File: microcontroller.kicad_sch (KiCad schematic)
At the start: 20 parts, among them SW1 A6S-2104-H, U6 STM32H725RGV6, Y1 ECS-2520MV-240-BN

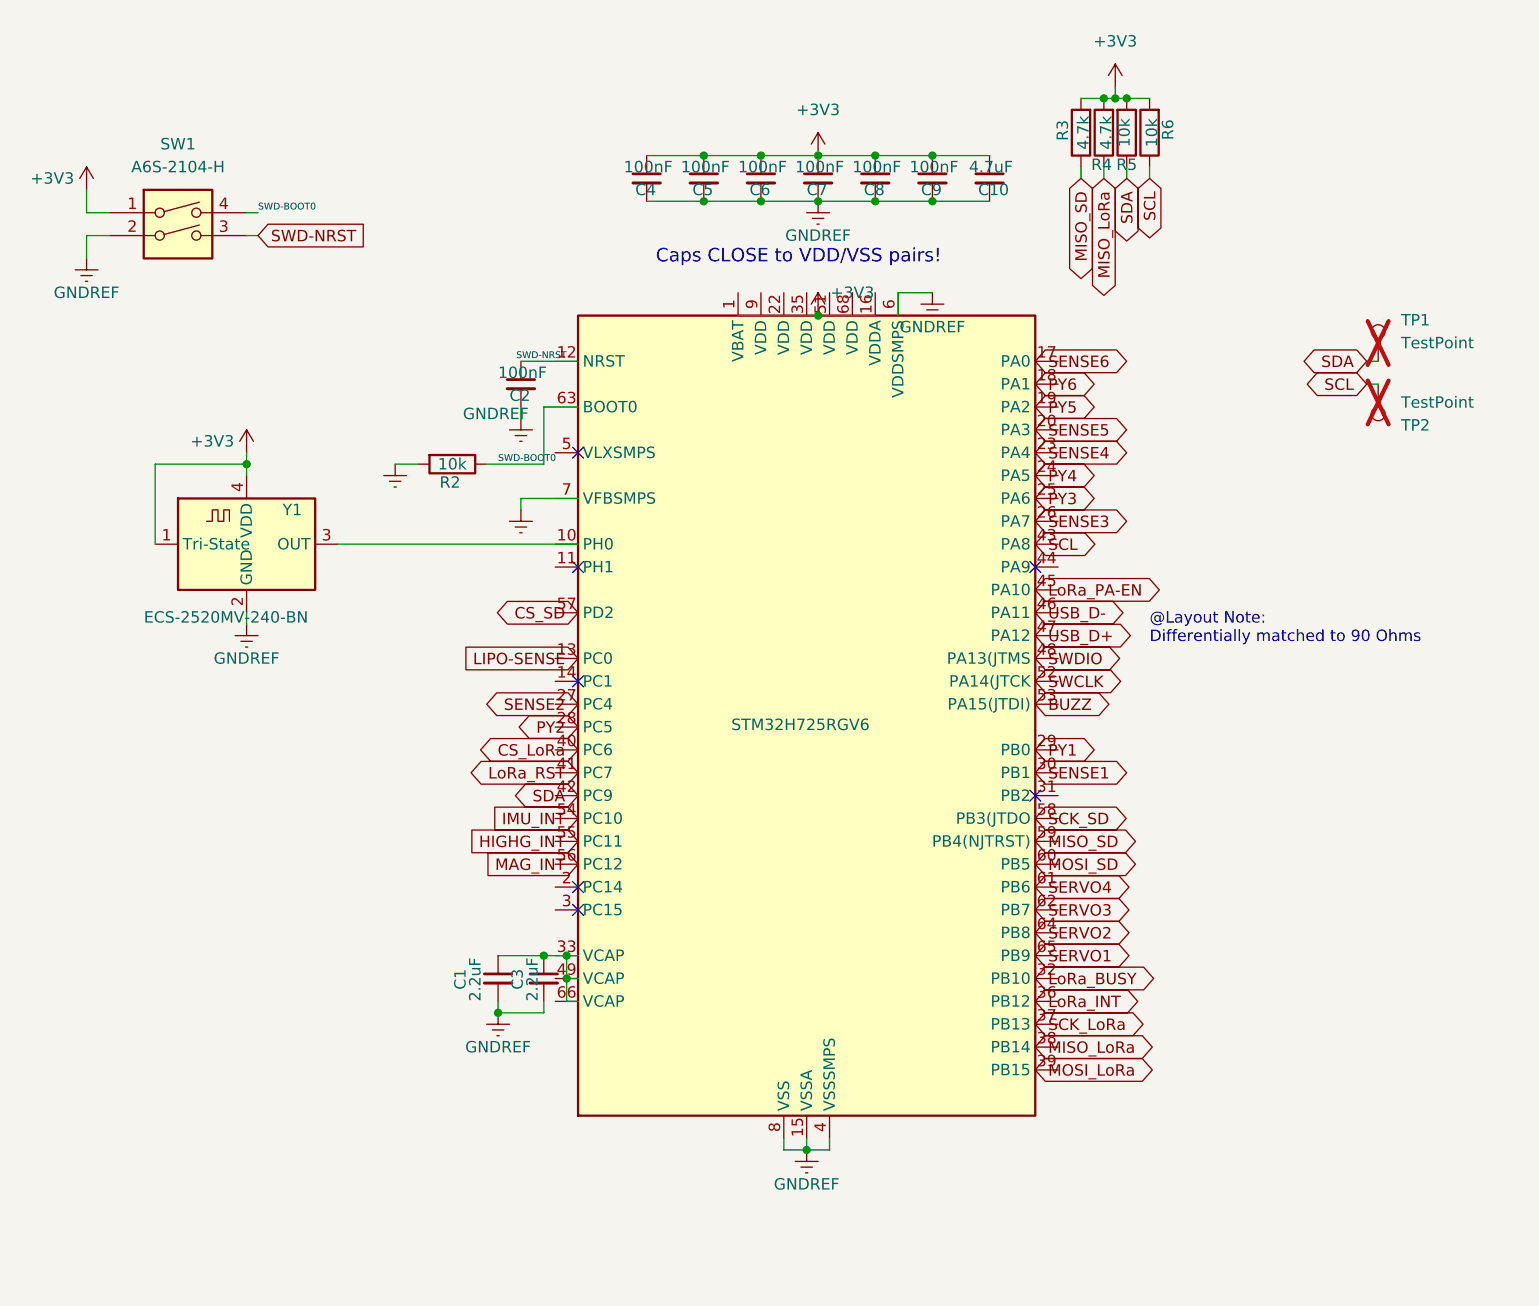
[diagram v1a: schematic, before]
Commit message: Added previously missing V_CORE 1.35V regulator
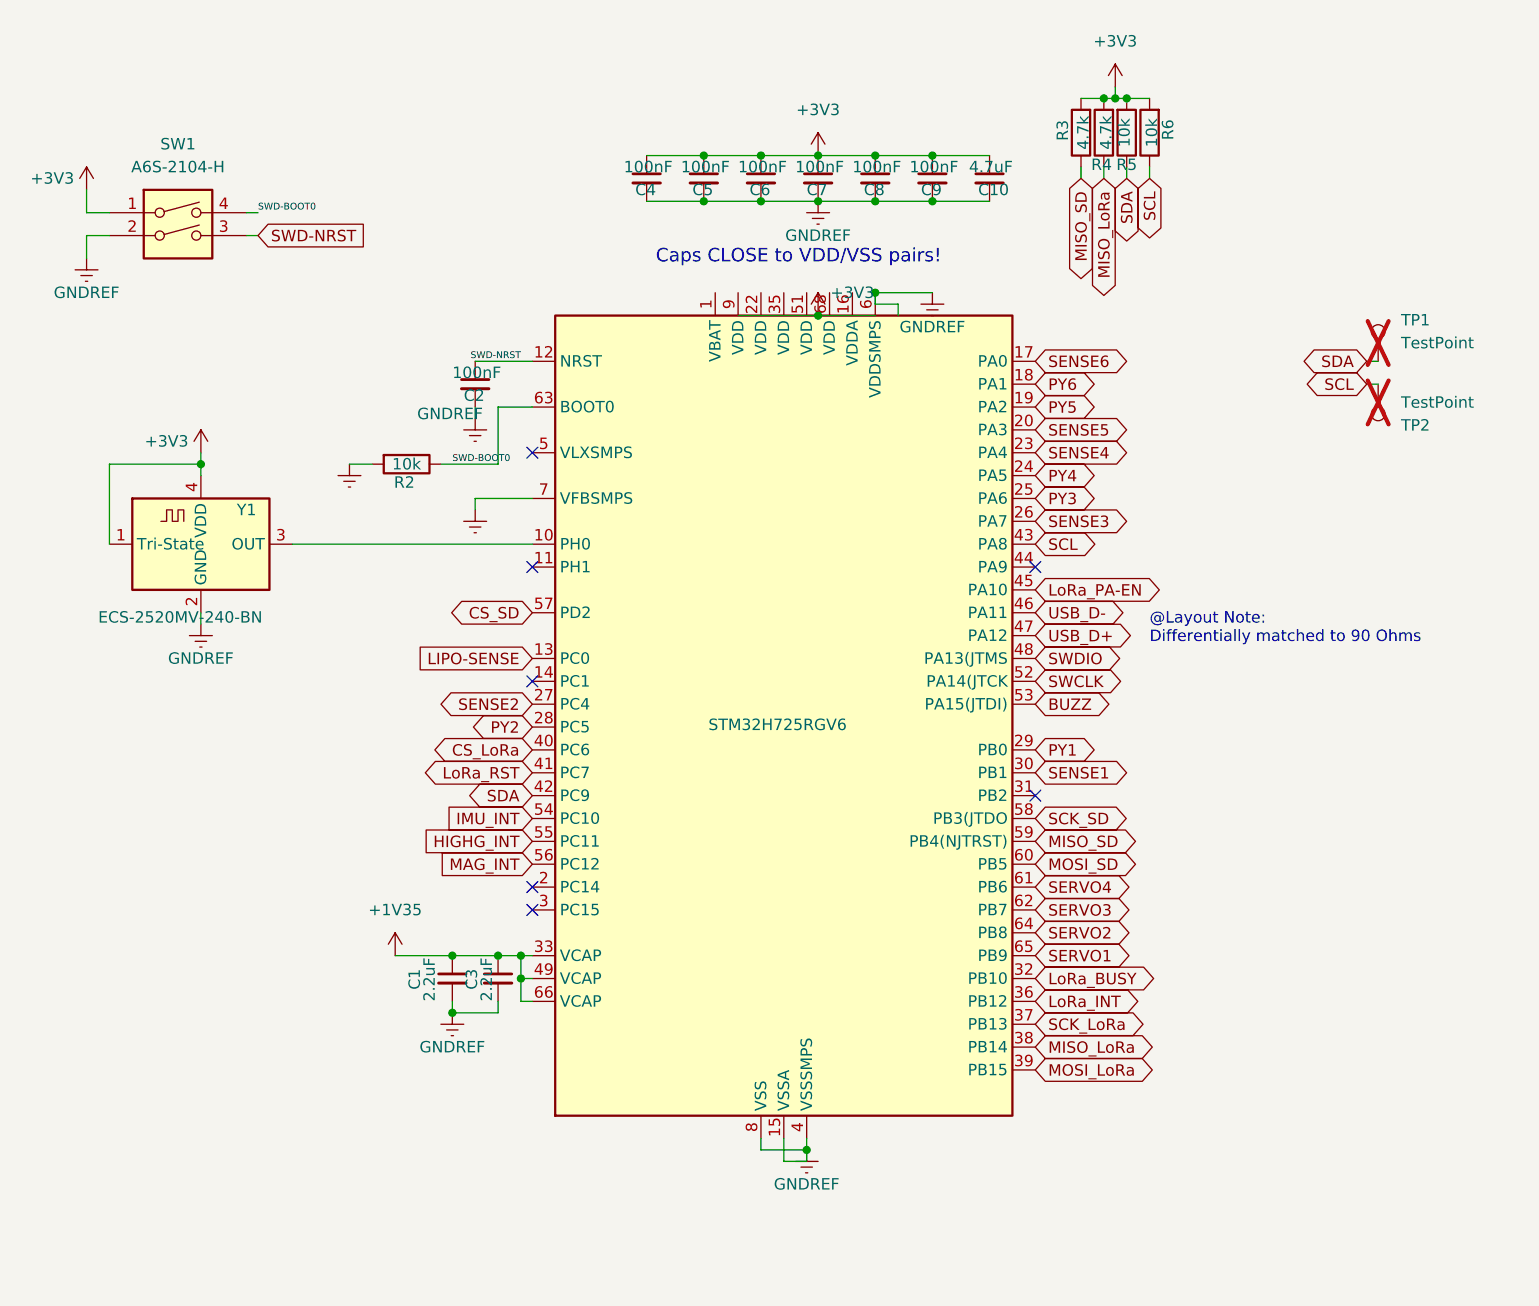
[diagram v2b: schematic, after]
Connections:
- net BUZZ: now also U6.53 (PA15(JTDI))
- net CS_LoRa: now also U6.40 (PC6)
- net CS_SD: now also U6.57 (PD2)
- net GNDREF: now also U6.7 (VFBSMPS)
- net HIGHG_INT: now also U6.55 (PC11)
- net IMU_INT: now also U6.54 (PC10)
- net LIPO-SENSE: now also U6.13 (PC0)
- net LoRa_BUSY: now also U6.32 (PB10)
- net LoRa_INT: now also U6.36 (PB12)
- net LoRa_PA-EN: now also U6.45 (PA10)
- net LoRa_RST: now also U6.41 (PC7)
- net MAG_INT: now also U6.56 (PC12)
- net MISO_LoRa: now also U6.38 (PB14)
- net MISO_SD: now also U6.59 (PB4(NJTRST))
- net MOSI_LoRa: now also U6.39 (PB15)
- net MOSI_SD: now also U6.60 (PB5)
- net PY1: now also U6.29 (PB0)
- net PY2: now also U6.28 (PC5)
- net PY3: now also U6.25 (PA6)
- net PY4: now also U6.24 (PA5)
- net PY5: now also U6.19 (PA2)
- net PY6: now also U6.18 (PA1)
- net SCK_LoRa: now also U6.37 (PB13)
- net SCK_SD: now also U6.58 (PB3(JTDO)
- net SCL: now also U6.43 (PA8)
- net SDA: now also U6.42 (PC9)
- net SENSE1: now also U6.30 (PB1)
- net SENSE2: now also U6.27 (PC4)
- net SENSE3: now also U6.26 (PA7)
- net SENSE4: now also U6.23 (PA4)
- net SENSE5: now also U6.20 (PA3)
- net SENSE6: now also U6.17 (PA0)
- net SERVO1: now also U6.65 (PB9)
- net SERVO2: now also U6.64 (PB8)
- net SERVO3: now also U6.62 (PB7)
- net SERVO4: now also U6.61 (PB6)
- net SWCLK: now also U6.52 (PA14(JTCK)
- net SWD-BOOT0: now also U6.63 (BOOT0)
- net SWD-NRST: now also U6.12 (NRST)
- net SWDIO: now also U6.48 (PA13(JTMS)
- net USB_D+: now also U6.47 (PA12)
- net USB_D-: now also U6.46 (PA11)
- net +1V35: now reaches C1.1, C3.1
- net +1V35: now also U6.33 (VCAP), U6.49 (VCAP), U6.66 (VCAP)
- net at U6.10 (PH0): now also Y1.3 (OUT)
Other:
- moved on the sheet: C1, C2, C3, R2, Y1

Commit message: Some layout tweaks
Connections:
- net +3V3: now also U6.1 (VBAT), U6.16 (VDDA), U6.22 (VDD), U6.35 (VDD), U6.51 (VDD), U6.68 (VDD), U6.9 (VDD)

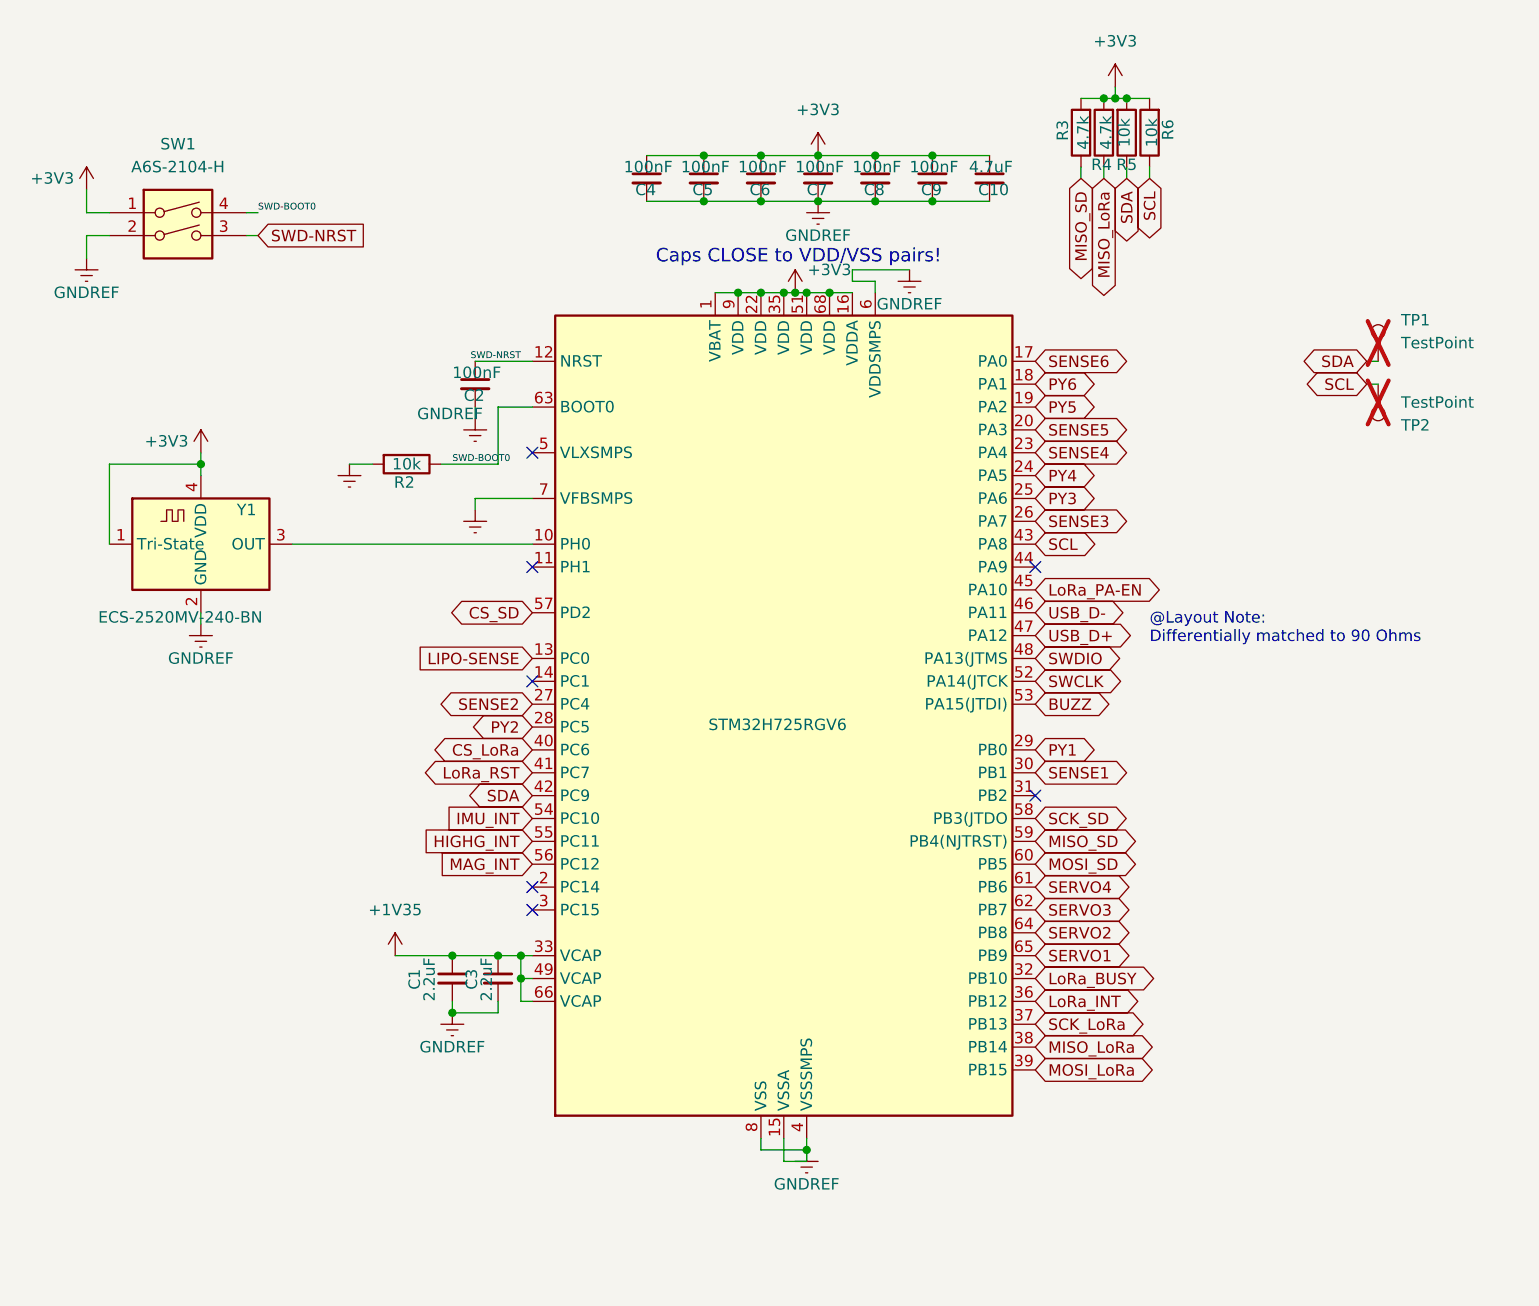
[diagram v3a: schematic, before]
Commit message: updated power delivery and component choices. v4 now ready
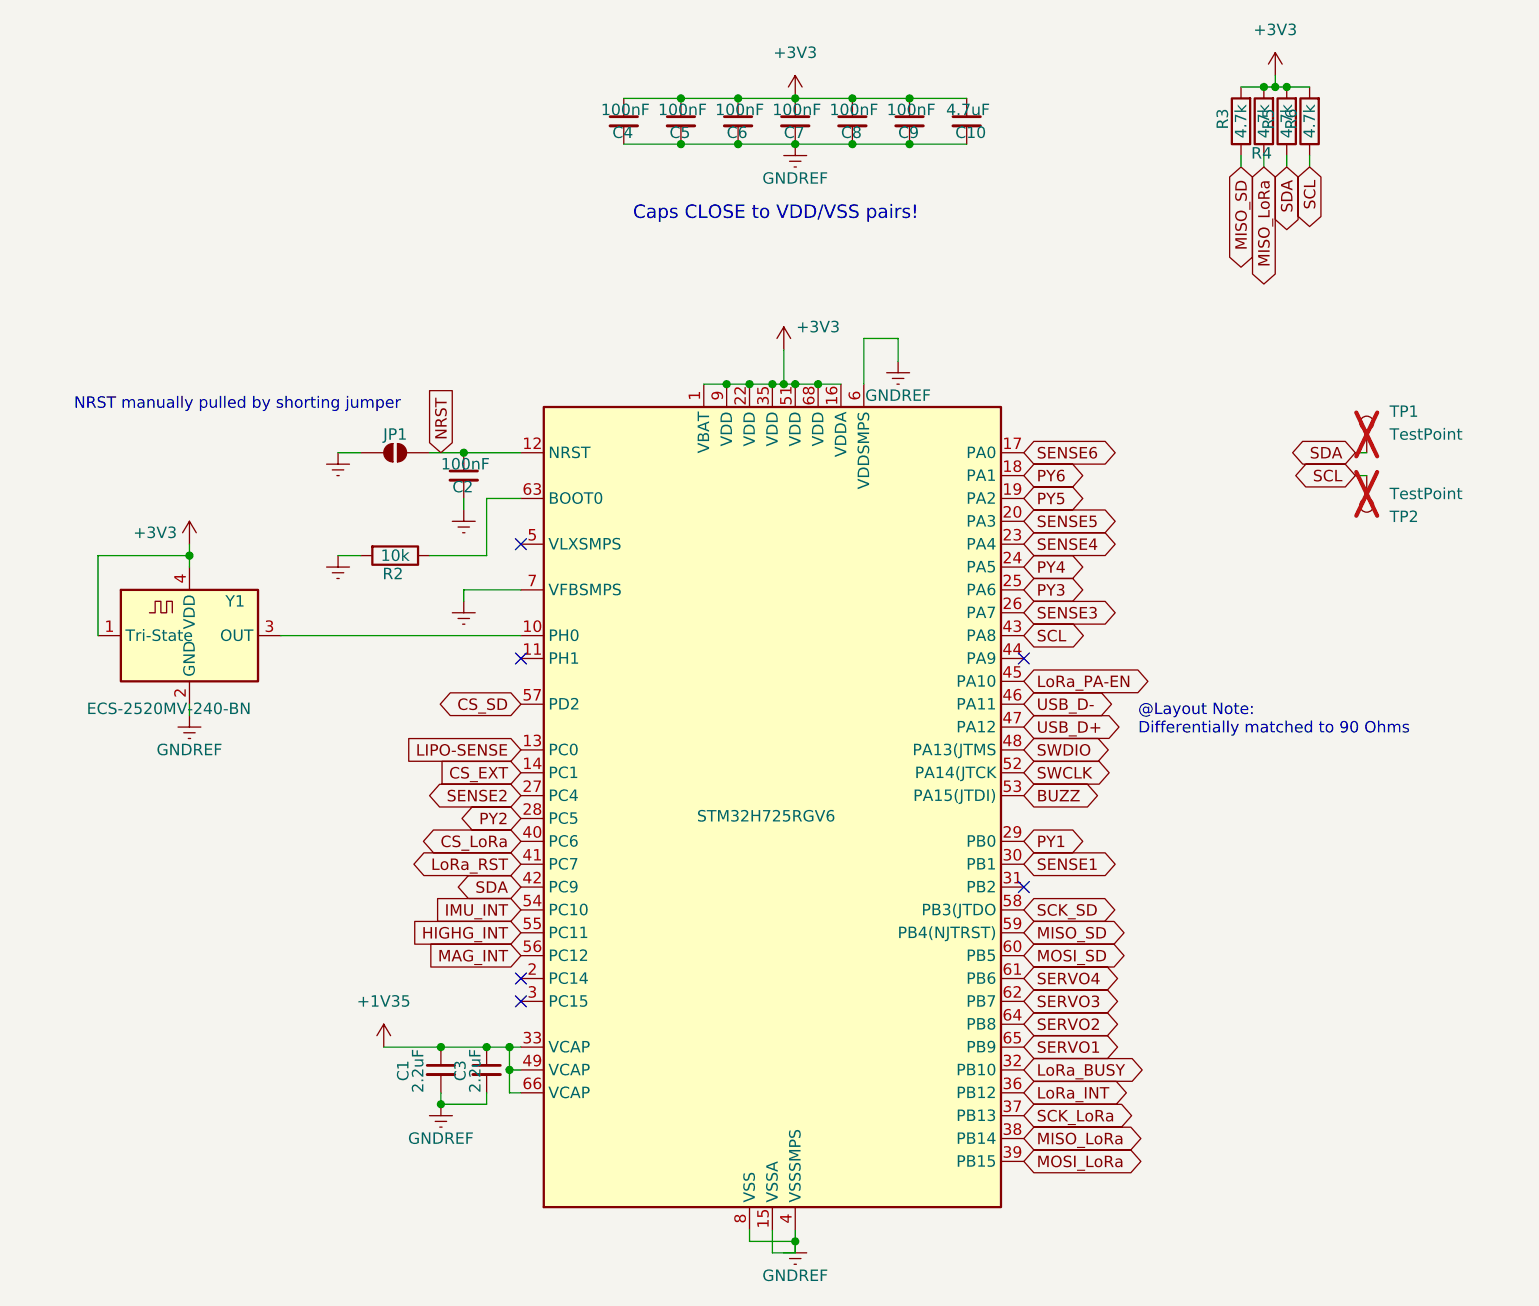
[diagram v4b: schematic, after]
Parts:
- removed SW1: A6S-2104-H, Button_Switch_SMD:SW_DIP_SPSTx02_Slide_Omron_A6S-210x_W8.9mm_P2.54mm, symbol Switch:SW_DIP_x02
- added JP1: SolderJumper_2_Open, Jumper:SolderJumper-2_P1.3mm_Open_RoundedPad1.0x1.5mm, symbol Jumper:SolderJumper_2_Open
- R5, R6: value 10k -> 4.7k; LCSC C25804 -> C23162; Product ID ERJ-PA3F1002V -> ERJ-PA3J472V
- U6: footprint Package_DFN_QFN:QFN-68-1EP_8x8mm_P0.4mm_EP6.4x6.4mm -> Package_DFN_QFN:QFN-68-1EP_8x8mm_P0.4mm_EP5.2x5.2mm
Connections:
- net GNDREF: now also JP1.1 (A)
- net CS_EXT: now reaches U6.14 (PC1)
- net SWD-BOOT0: no longer names the net of R2.1, U6.63 (BOOT0)
- net SWD-NRST renamed NRST
- net NRST: now also JP1.2 (B)
- no-connect marks 7 -> 6
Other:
- note added: "NRST manually pulled by shorting jumper"
- moved on the sheet: C1, C10, C2, C3, C4, C5, C6, C7, C8, C9, R2, R3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

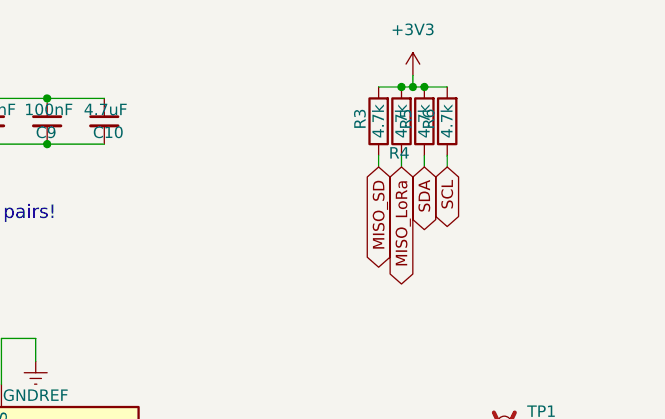
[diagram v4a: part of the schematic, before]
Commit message: Fixed power distribution and made small improvements. Updated revision number
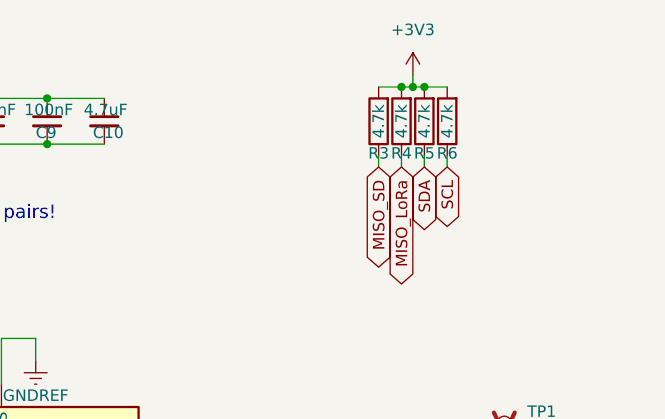
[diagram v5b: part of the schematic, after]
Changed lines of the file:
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@@
 	(title_block
 		(title "WINTER Microcontroller Layout")
-		(date "2025-08-28")
-		(rev "4-Dev")
+		(date "2025-11-24")
+		(rev "4.1")
 		(company "SparrowTheNerd")
 	)
